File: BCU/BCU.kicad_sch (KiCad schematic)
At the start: 59 parts, among them IC1 STM32G474RET6, IC2 TJA1042T_3,118, IC3 LM317MDCYR, IC4 LTC6820HUD#PBF, Y1 NX2520SA-24.000000MHZ-B8

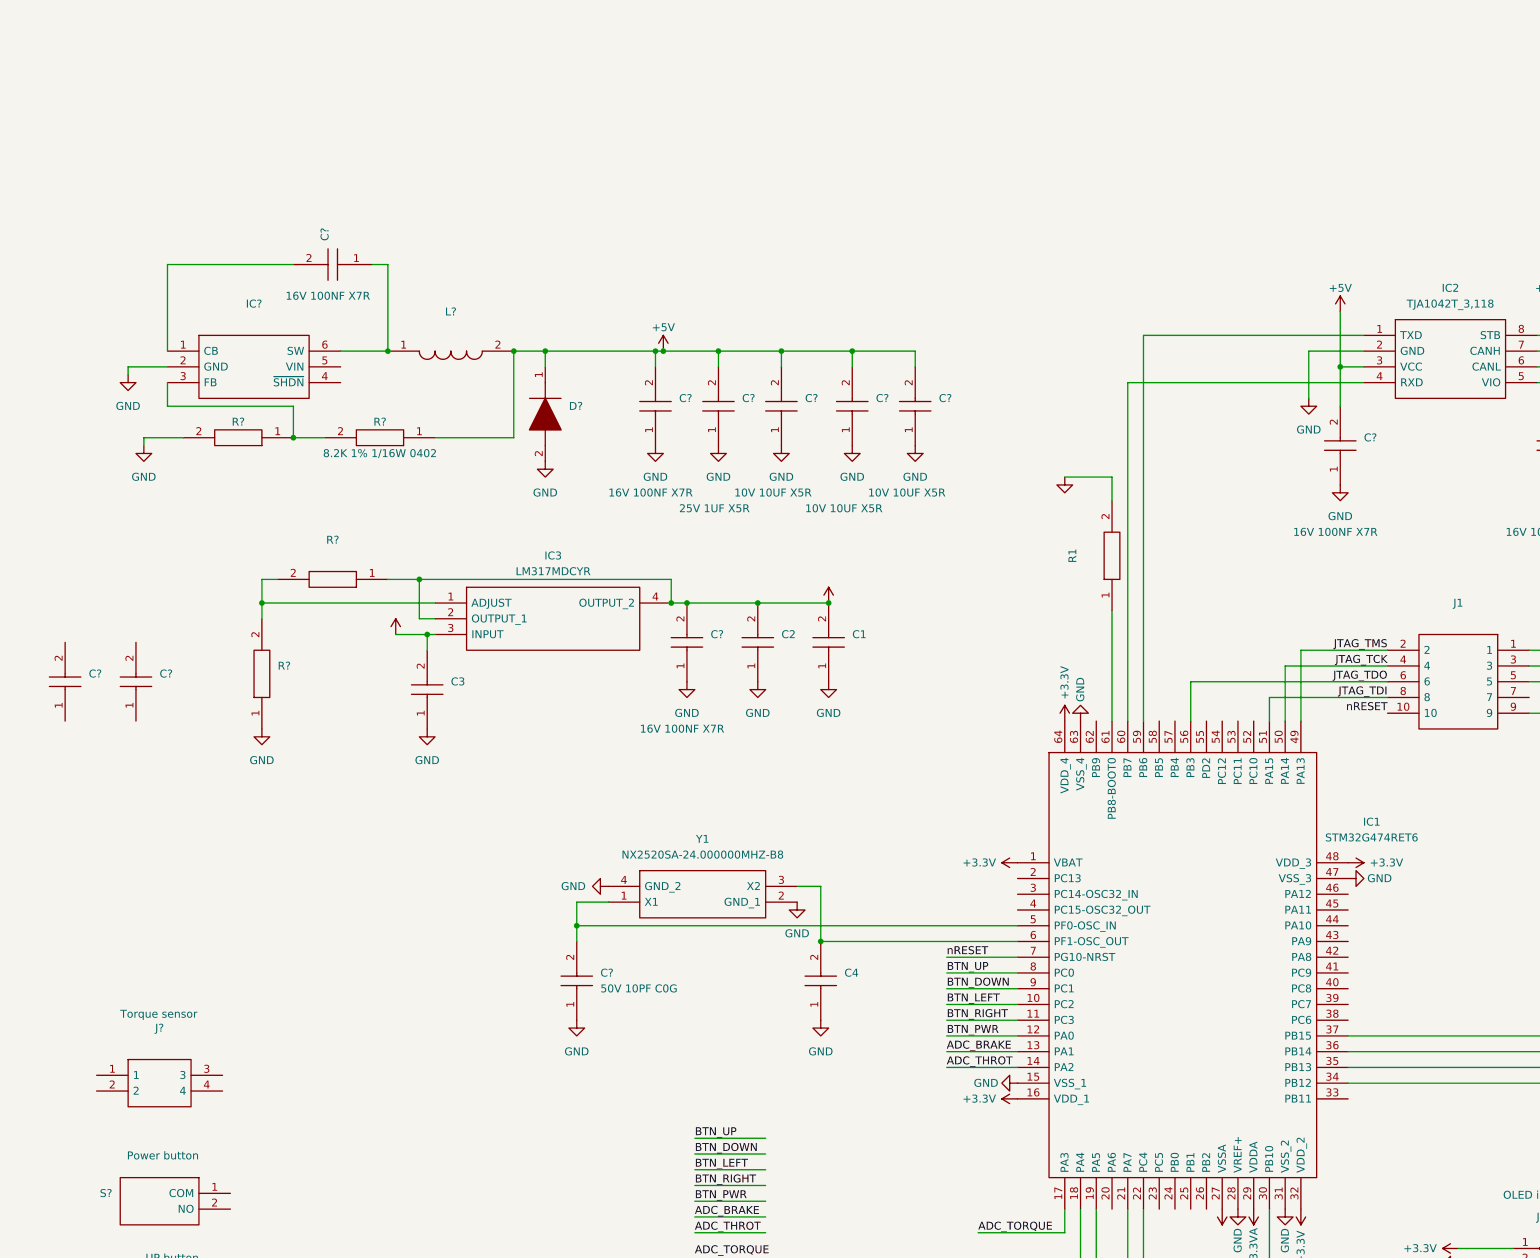
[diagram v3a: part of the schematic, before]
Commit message: Update BCU.kicad_sch
added HV power supply
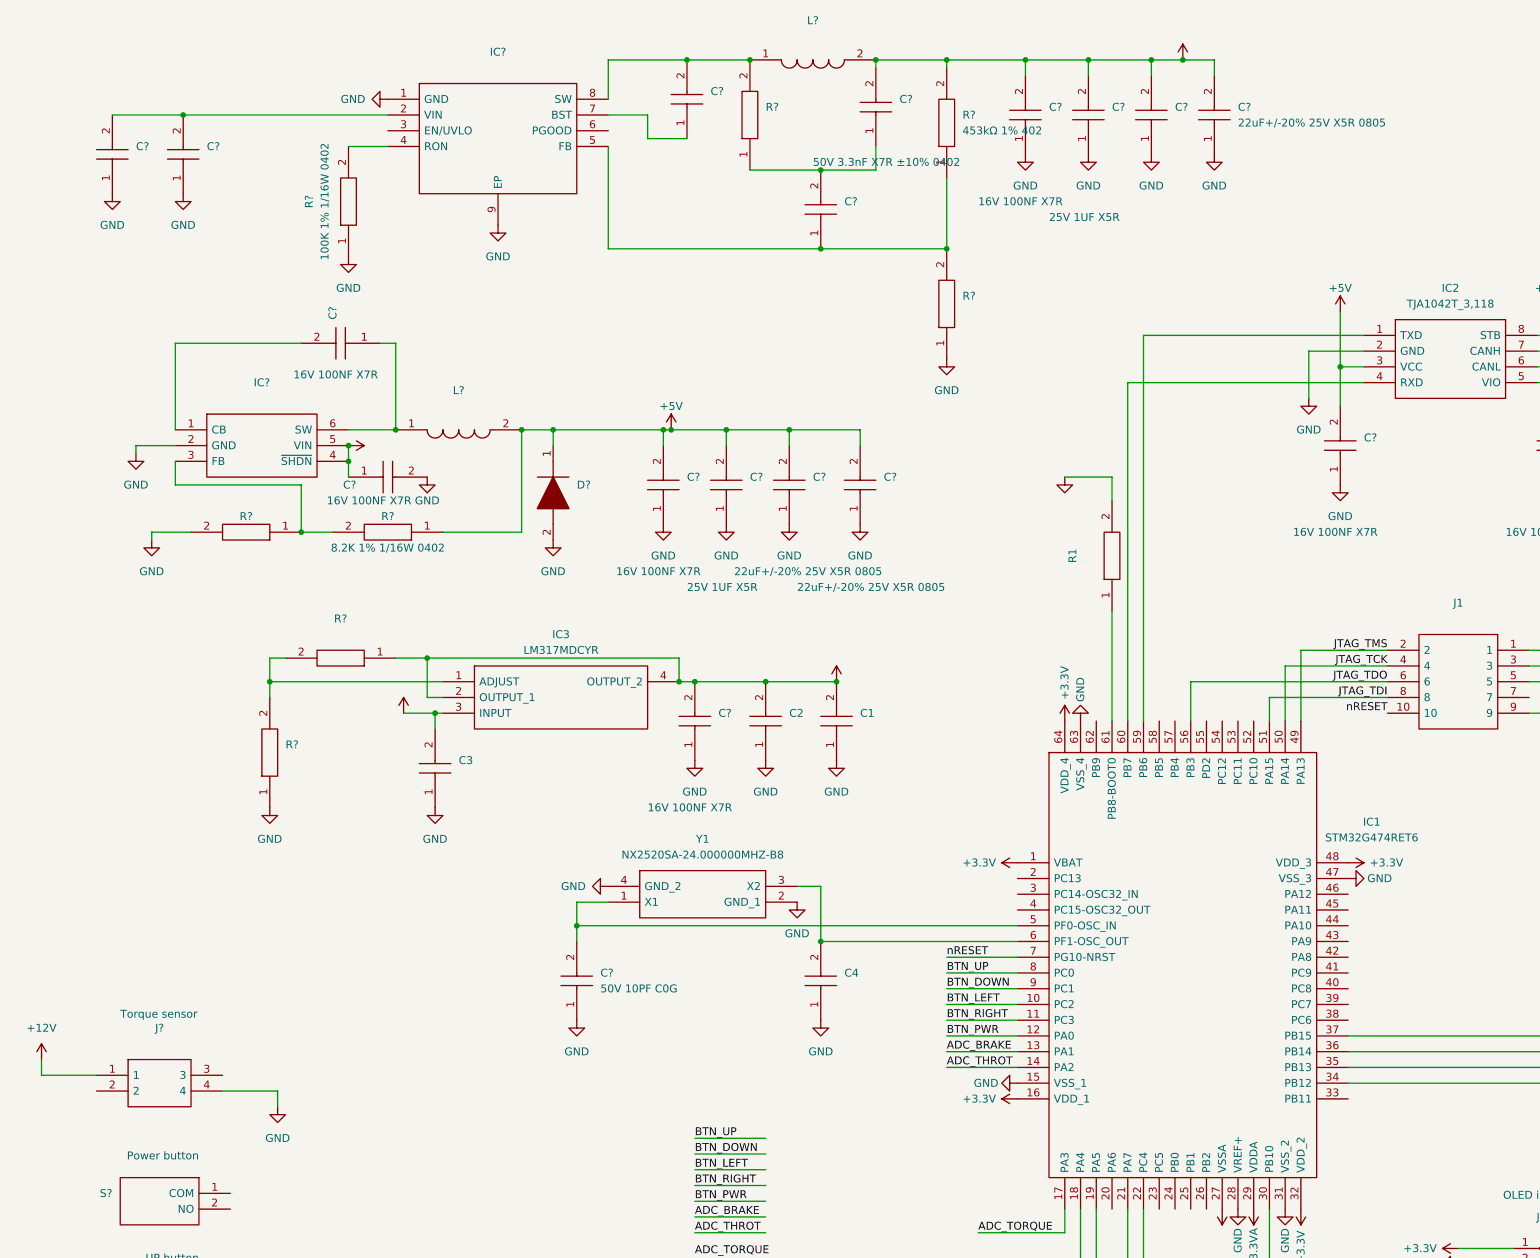
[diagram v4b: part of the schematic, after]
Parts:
- removed C?: (no value), symbol SamacSys_Parts:CL05B104KB54PNC
- removed C?: (no value), symbol SamacSys_Parts:GRM21BR61H106KE43L
- removed C? (x3): 10V 10UF X5R, CAPC1608X90N, symbol SamacSys_Parts:CL10A106KP8NNNC
- added C?: (no value), symbol SamacSys_Parts:GRM31CC72A475KE11L
- added C? (x2): 16V 100NF X7R, CAPC1005X55N, symbol SamacSys_Parts:CL05B104KO5NNNC
- added C?: (no value), symbol SamacSys_Parts:CL21B104KCFNNNE
- added C?: (no value), symbol SamacSys_Parts:CL05B332KB5NNNC
- added C?: 50V 3.3nF X7R ±10% 0402, CAPC1005X55N, symbol SamacSys_Parts:CL05B332KB5NNNC
- added C?: (no value), symbol SamacSys_Parts:CL21A226MAYNNNE
- added C?: (no value), symbol SamacSys_Parts:CC0402GRNPO9BN560
- added C? (x3): 22uF+/-20% 25V X5R 0805, CAPC2012X145N, symbol SamacSys_Parts:CL21A226MAYNNNE
- added C?: 25V 1UF X5R, CAPC1005X60N, symbol SamacSys_Parts:CL05A105KA5NQNC
- added IC?: (no value), symbol SamacSys_Parts:LM5164DDAR
- added L?: (no value), symbol SamacSys_Parts:SLF7045T-680MR60-PF
- added R?: 453kΩ 1% 402, RESC1005X40N, symbol SamacSys_Parts:RC0402FR-07453KL
- added R?: (no value), symbol SamacSys_Parts:0402WGF1002TCE
- added R?: 100K 1% 1/16W 0402, RESC1005X40N, symbol SamacSys_Parts:0402WGF1003TCE
- added R?: (no value), symbol SamacSys_Parts:RC0402FR-07453KL
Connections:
- net +5V: now also C?.2, C?.2
- net GND: now also J?.4, C?.1, C?.1, C?.1, C?.1, C?.1, C?.1, C?.1, C?.1, C?.2, IC?.1 (GND), IC?.9 (EP), R?.1, R?.1
- net +12V: now reaches J?.1
- net +12V: now also IC?.4 (~{SHDN}), IC?.5 (VIN), C?.1, C?.2, C?.2, C?.2, C?.2, C?.2, L?.2, R?.2
- new net: C?.1, IC?.5 (FB), R?.1, R?.2
- new net: C?.2, C?.2, IC?.2 (VIN)
- new net: C?.2, IC?.8 (SW), L?.1, R?.2
- new net: IC?.4 (RON), R?.2
- new net: C?.1, IC?.7 (BST)
- new net: C?.1, C?.2, R?.1
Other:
- moved on the sheet: C1, C2, C3, C?, D?, IC3, IC?, L?, R?

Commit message: update pcb+sch
pushed to pcb
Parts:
- gave numbers to parts that had none: 61
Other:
- note added: "NOTES Check if part from JLC will fit USBC footprint https://datasheet.lcsc.com/lcsc/2108131730_Korean-Hroparts-Elec-TYPE-C-31-M-12_C165948.pdf check vesc shutdown signal add an sd card add uart for TI bmbs"
- note removed: "Check if part from JLC will fit https://datasheet.lcsc.com/lcsc/2108131730_Korean-Hroparts-Elec-TYPE-C-31-M-12_C165948.pdf"

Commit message: Migrate schemtaic to coilchain library
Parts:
- removed C1: (no value), symbol SamacSys_Parts:CL10A106KP8NNNC
- removed C10, C12, C18, C19, C20, C21, C23, C25, C27, C28, C30, C31, C32, C7, C8: 16V 100NF X7R, CAPC1005X55N, symbol SamacSys_Parts:CL05B104KO5NNNC
- removed C11: (no value), symbol SamacSys_Parts:CL05B332KB5NNNC
- removed C13, C22, C29: 25V 1UF X5R, CAPC1005X60N, symbol SamacSys_Parts:CL05A105KA5NQNC
- removed C14, C16, C26: 22uF+/-20% 25V X5R 0805, CAPC2012X145N, symbol SamacSys_Parts:CL21A226MAYNNNE
- removed C15: (no value), symbol SamacSys_Parts:CC0402GRNPO9BN560
- removed C17: 50V 3.3nF X7R ±10% 0402, CAPC1005X55N, symbol SamacSys_Parts:CL05B332KB5NNNC
- removed C2: (no value), symbol SamacSys_Parts:CL05A105KA5NQNC
- removed C24: (no value), symbol SamacSys_Parts:CL21A226MAYNNNE
- removed C3: (no value), symbol SamacSys_Parts:CL05B104KO5NNNC
- removed C4: (no value), symbol SamacSys_Parts:CL05C100JB5NNNC
- removed C5: (no value), symbol SamacSys_Parts:GRM31CC72A475KE11L
- removed C6: (no value), symbol SamacSys_Parts:CL21B104KCFNNNE
- removed C9: 50V 10PF C0G, CAPC1005X55N, symbol SamacSys_Parts:CL05C100JB5NNNC
- removed D1: (no value), symbol SamacSys_Parts:MBR140SFT1G
- removed FB1: BLM15HD182SN1D, NFZ15SG152SN10B, symbol SamacSys_Parts:BLM15HD182SN1D
- removed H1: (no value), symbol Mechanical:MountingHole
- removed H2, H3, H4: MountingHole, MountingHole:MountingHole_2.2mm_M2, symbol Mechanical:MountingHole
- removed IC1: STM32G474RET6, QFP50P1200X1200X160-64N, symbol SamacSys_Parts:STM32G474RET6
- removed IC2: TJA1042T_3,118, SOIC127P600X175-8N, symbol SamacSys_Parts:TJA1042T_3,118
- removed IC3: LM317MDCYR, SOT230P700X180-4N, symbol SamacSys_Parts:LM317MDCYR
- removed IC4: LTC6820HUD#PBF, QFN50P300X300X80-17N-D, symbol SamacSys_Parts:LTC6820HUD#PBF
- removed IC5: (no value), symbol SamacSys_Parts:LM2842YQMK_NOPB
- removed IC6: (no value), symbol SamacSys_Parts:LM5164DDAR
- removed J1: (no value), FTSH-105-XX-YYY-DV-K-P-TR, symbol SamacSys_Parts:FTSH-105-01-F-DV-K-P-TR
- removed J2, J4, J5: (no value), symbol SamacSys_Parts:SM04B-PASS-TBT_LF__SN_
- removed J3: (no value), symbol Connector:Conn_01x07_Male
- removed J6: (no value), symbol Connector:USB_C_Receptacle_USB2.0
- removed L1: (no value), symbol SamacSys_Parts:CBC3225T680KRV
- removed L2: (no value), symbol SamacSys_Parts:SLF7045T-680MR60-PF
- removed R1: (no value), symbol SamacSys_Parts:0402WGF1003TCE
- removed R10, R3, R5: (no value), symbol SamacSys_Parts:0402WGF8201TCE
- removed R11, R12, R13: 51R 1% 1/16W 0402, RESC1005X40N, symbol SamacSys_Parts:0402WGF8201TCE
- removed R2, R9: (no value), symbol SamacSys_Parts:0402WGF1002TCE
- removed R4: 100K 1% 1/16W 0402, RESC1005X40N, symbol SamacSys_Parts:0402WGF1003TCE
- removed R6: 8.2K 1% 1/16W 0402, RESC1005X40N, symbol SamacSys_Parts:0402WGF8201TCE
- removed R7: (no value), symbol SamacSys_Parts:RC0402FR-07453KL
- removed R8: 453kΩ 1% 402, RESC1005X40N, symbol SamacSys_Parts:RC0402FR-07453KL
- removed S1: (no value), symbol SamacSys_Parts:TS-1101-C-W
- removed S2, S3, S4, S5: TS-1101-C-W, TS1101CW, symbol SamacSys_Parts:TS-1101-C-W
- removed T1: (no value), symbol SamacSys_Parts:PE-68386NLT
- removed Y1: NX2520SA-24.000000MHZ-B8, NX2520SA24000000MHZB8, symbol SamacSys_Parts:NX2520SA-24.000000MHZ-B8
- added H? (x4): MountingHole, MountingHole:MountingHole_2.2mm_M2, symbol Mechanical:MountingHole
- added J?: USB_C_Receptacle_USB2.0, symbol Connector:USB_C_Receptacle_USB2.0
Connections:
- net GND: now also J?.A1 (GND), J?.A12 (GND), J?.B1 (GND), J?.B12 (GND), J?.S1 (SHIELD)
- new net: J?.A4 (VBUS), J?.A9 (VBUS), J?.B4 (VBUS), J?.B9 (VBUS)
- new net USB_D+: J?.A6 (D+), J?.B6 (D+)
- new net USB_D-: J?.A7 (D-), J?.B7 (D-)
- no-connect marks 0 -> 4
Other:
- added sheet battery (battery.kicad_sch)
- added sheet can (can.kicad_sch)
- added sheet mcu (mcu.kicad_sch)
- added sheet power (power.kicad_sch)
- added sheet sensors (sensors.kicad_sch)
- added sheet ui (ui.kicad_sch)
- note added: "Coilchain BCU Schematic"
- note added: "NOTES Check if part from JLC will fit USBC footprint https://datasheet.lcsc.com/lcsc/2108131730_Korean-Hroparts-Elec-TYPE-C-31-M-12_C165948.pdf check vesc shutdown signal add an sd card add uart for TI bmbs Shield USB to a damping RC network"
- note removed: "Battery connection"
- note removed: "DOWN button"
- note removed: "LEFT button"
- note removed: "NOTES Check if part from JLC will fit USBC footprint https://datasheet.lcsc.com/lcsc/2108131730_Korean-Hroparts-Elec-TYPE-C-31-M-12_C165948.pdf check vesc shutdown signal add an sd card add uart for TI bmbs"
- note removed: "OLED interface"
- note removed: "Power button"
- note removed: "RIGHT button"
- note removed: "Torque sensor"
- note removed: "UP button"
- note removed: "VESC connection"
- company: (none) -> Coilchain
- title: (none) -> Main

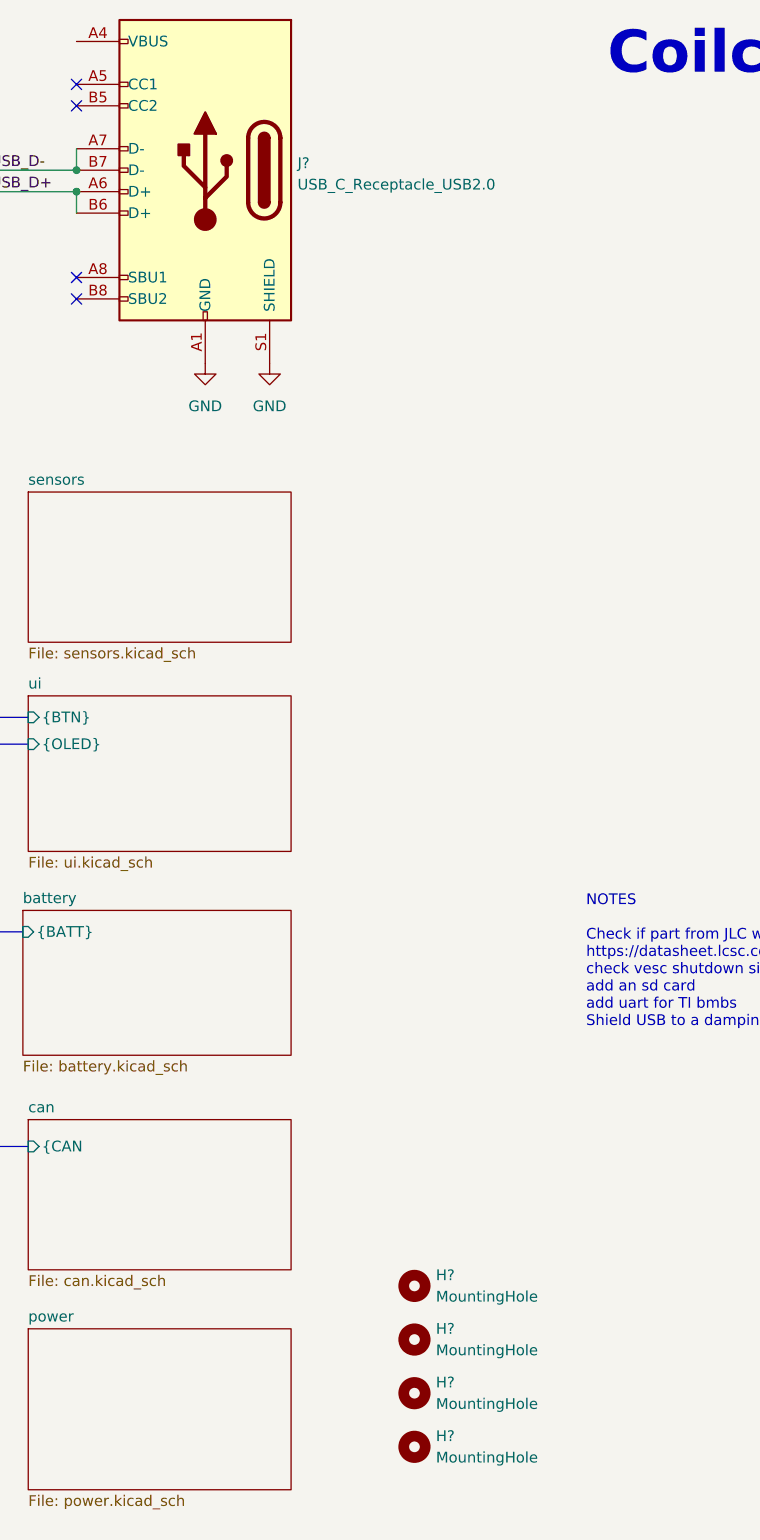
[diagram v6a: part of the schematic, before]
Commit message: Make rough component placement for evaluating missing 3D
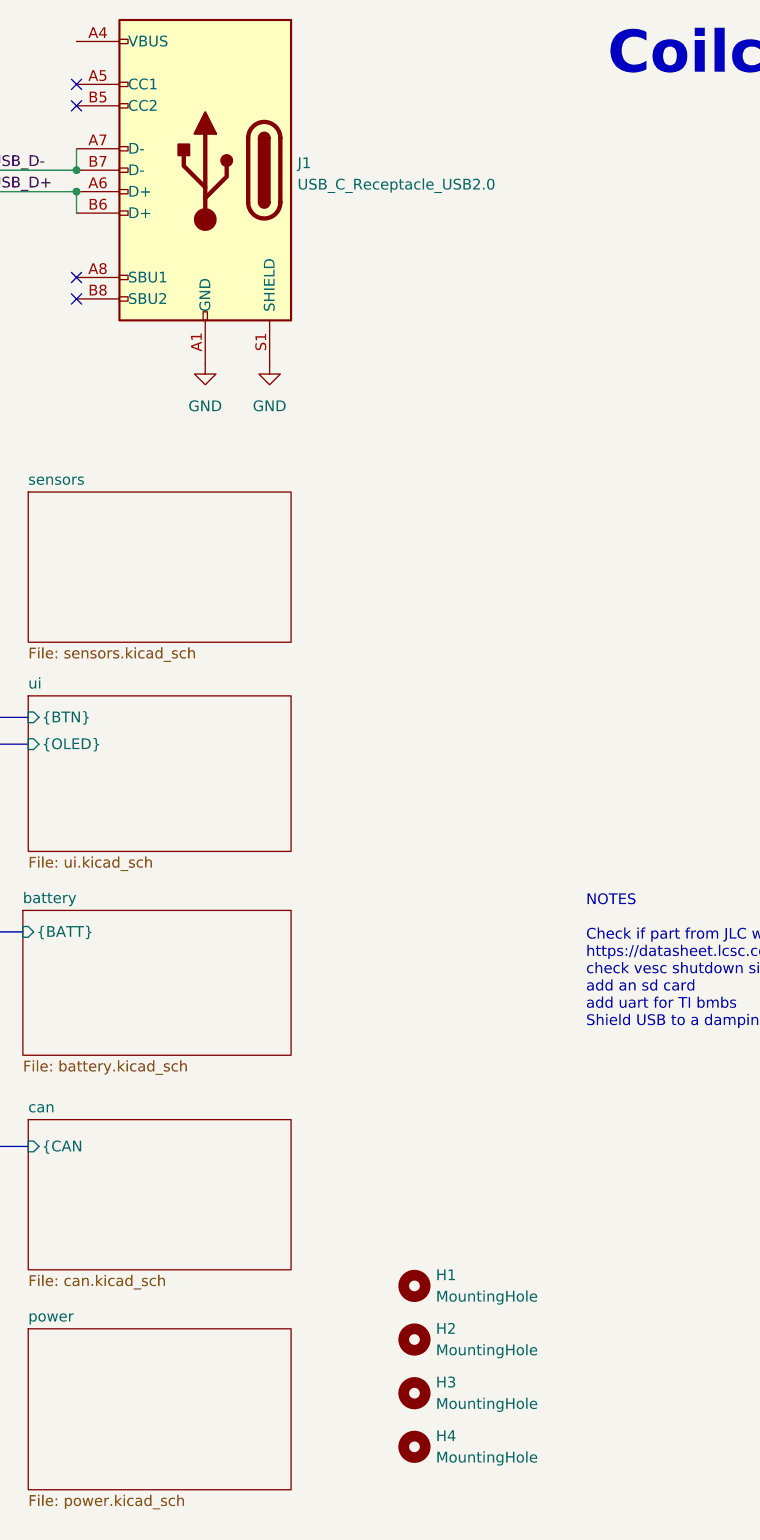
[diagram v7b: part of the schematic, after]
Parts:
- J1: renamed from J?; footprint (none) -> Connector_USB:USB_C_Receptacle_HRO_TYPE-C-31-M-12
- gave numbers to parts that had none: 4
